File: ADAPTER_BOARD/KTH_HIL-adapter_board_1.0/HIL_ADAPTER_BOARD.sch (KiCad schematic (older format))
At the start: 4 parts, among them CN10 Conn_02x20_Odd_Even, CN11 Conn_02x36_Odd_Even, CN12 Conn_02x36_Odd_Even, CN7 Conn_02x20_Odd_Even

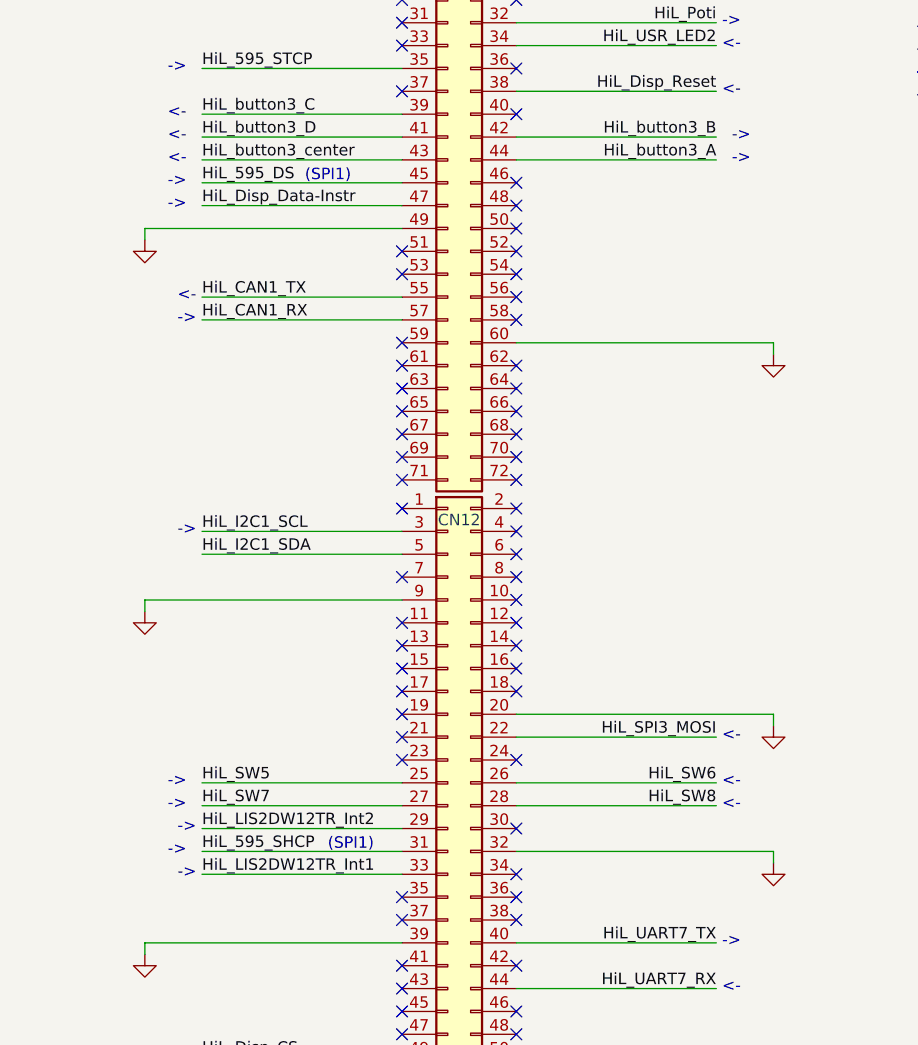
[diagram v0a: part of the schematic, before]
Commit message: Fixed comments regarding schematic
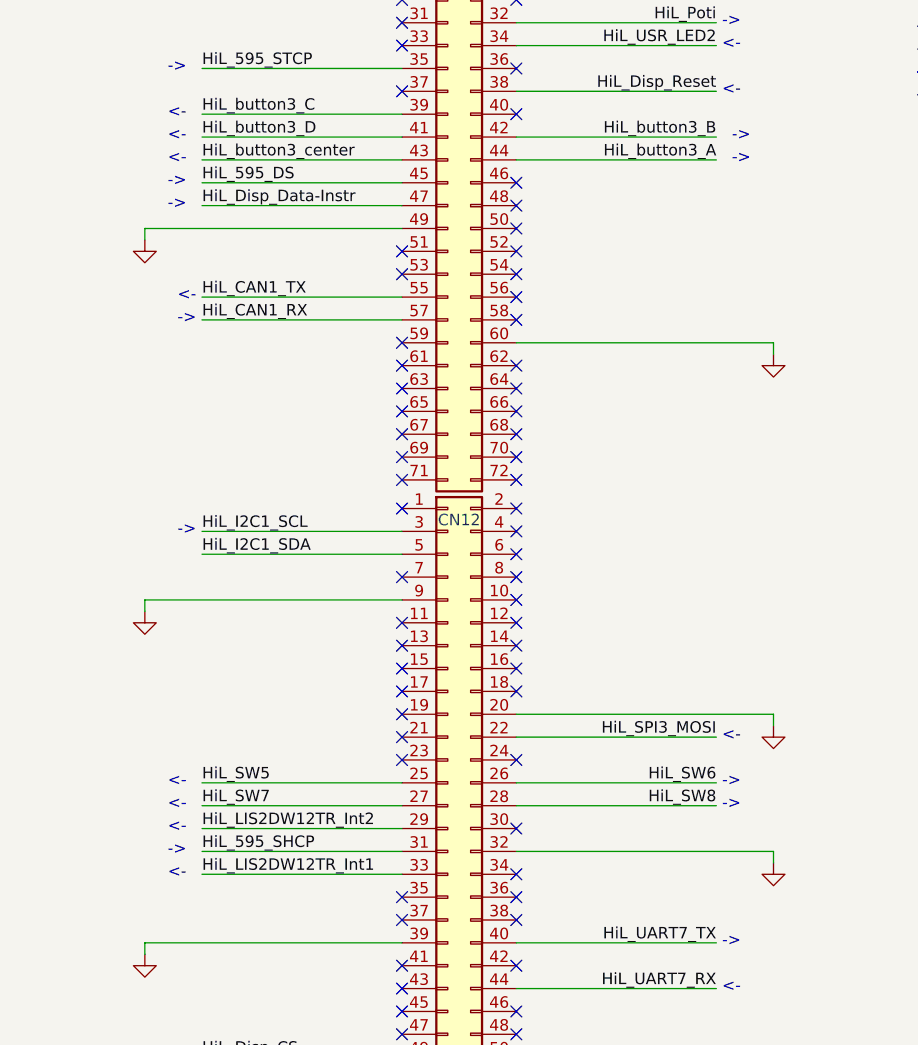
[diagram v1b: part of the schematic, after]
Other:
- note removed: "(SPI1)"
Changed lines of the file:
@@
 EESchema Schematic File Version 4
-LIBS:HIL_ADAPTER_BOARD-cache
 EELAYER 30 0
 EELAYER END
@@
 Text Notes 800  5725 0    50   ~ 0
 ->
-Text Notes 1500 5700 0    50   ~ 0
-(SPI1)
 Text Label 950  2775 0    50   ~ 0
 HiL_595_DS
@@
 Text Notes 800  2800 0    50   ~ 0
 ->
-Text Notes 1400 2775 0    50   ~ 0
-(SPI1)
 Text Label 3200 1875 2    50   ~ 0
 HiL_USR_LED1
@@
 Wire Wire Line
 	3200 5400 2325 5400
-Text Notes 3225 5425 0    50   ~ 0
-<-
 Text Label 3200 5500 2    50   ~ 0
 HiL_SW8
 Wire Wire Line
 	3200 5500 2325 5500
-Text Notes 3225 5525 0    50   ~ 0
-<-
 Text Label 950  6600 0    50   ~ 0
 HiL_Disp_CS
@@
 Wire Wire Line
 	1825 5600 950  5600
-Text Notes 925  5825 2    50   ~ 0
-->
-Text Notes 925  5625 2    50   ~ 0
-->
 Text Label 3200 5200 2    50   ~ 0
 HiL_SPI3_MOSI
@@
 Wire Wire Line
 	950  5500 1825 5500
-Text Notes 800  5525 0    50   ~ 0
-->
 Text Label 950  5500 0    50   ~ 0
 HiL_SW7
 Wire Wire Line
 	950  5400 1825 5400
-Text Notes 800  5425 0    50   ~ 0
-->
 Text Label 950  5400 0    50   ~ 0
 HiL_SW5
@@
 NoConn ~ 1825 2375
 NoConn ~ -2500 5250
+Text Notes 800  5425 0    50   ~ 0
+<-
+Text Notes 800  5525 0    50   ~ 0
+<-
+Text Notes 3225 5425 0    50   ~ 0
+->
+Text Notes 3225 5525 0    50   ~ 0
+->
+Text Notes 800  5625 0    50   ~ 0
+<-
+Text Notes 800  5825 0    50   ~ 0
+<-
 $EndSCHEMATC
